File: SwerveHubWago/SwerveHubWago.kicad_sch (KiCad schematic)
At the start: 5 parts, among them J1 2601-1110, J2 2601-1104, J3 15-91-3024

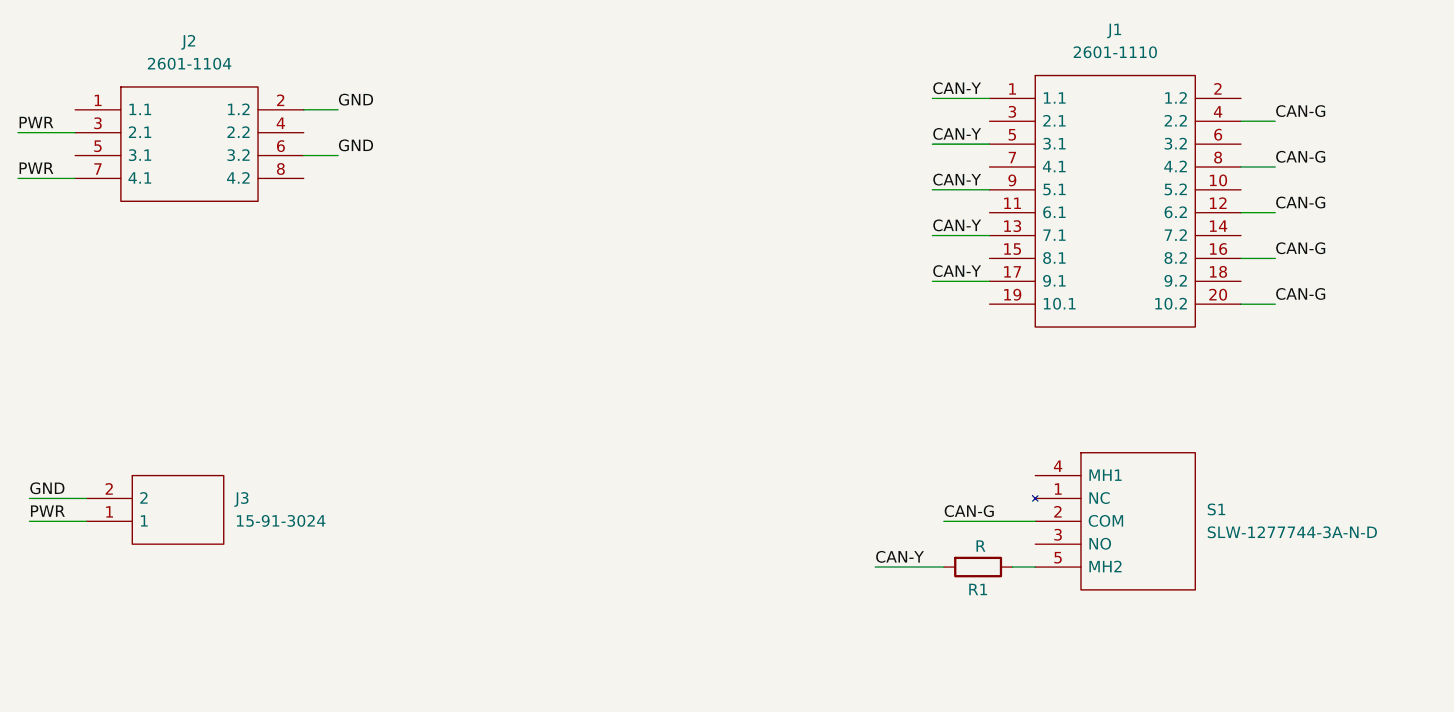
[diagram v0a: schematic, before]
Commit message: Rev 2
Switched connecters to two (in/out) Molex SL connectors for CAN and one three pin Molex SL connector for power. Changed Wago terminal blocks to 6 position for CAN and 2 position for power.
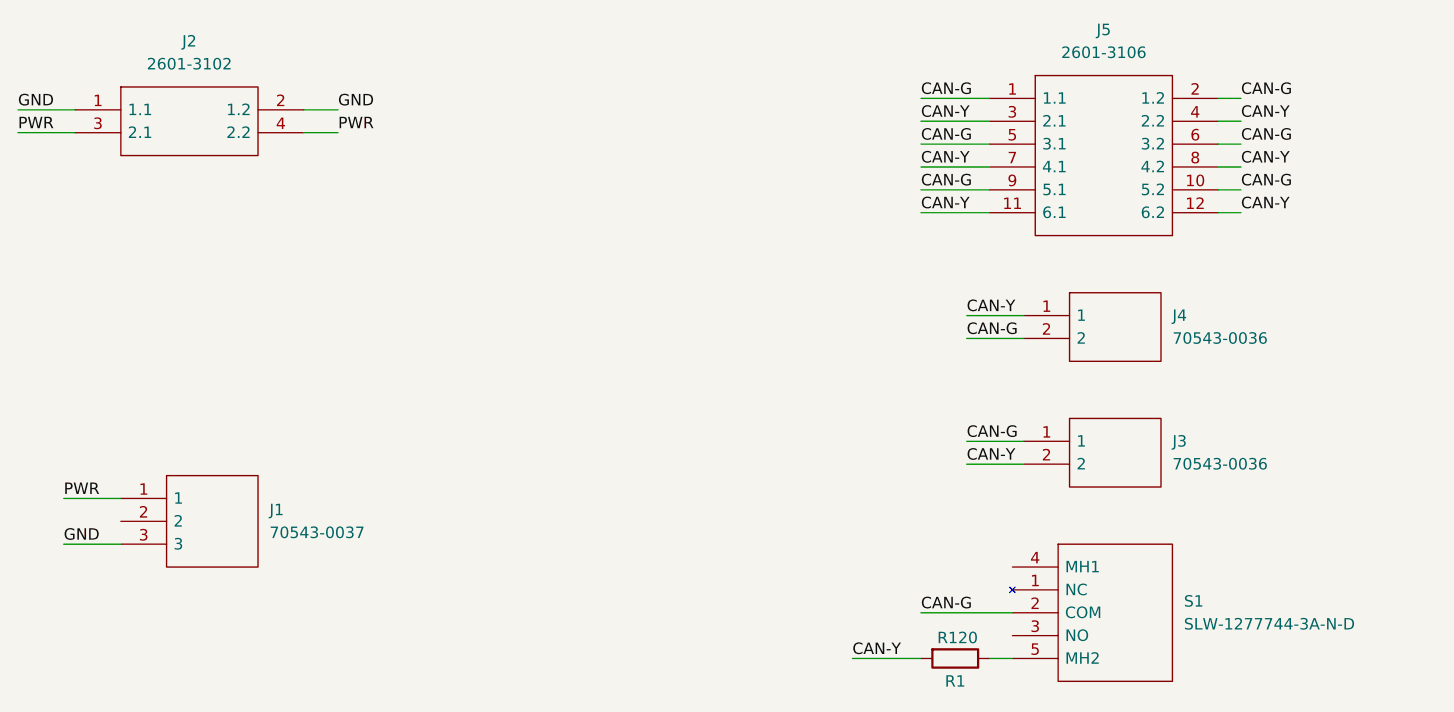
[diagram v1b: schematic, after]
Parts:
- removed J1: 2601-1110, SamacSys_Parts:26011110, symbol SamacSys_Parts:2601-1110
- removed J2: 2601-1104, SamacSys_Parts:26011104, symbol SamacSys_Parts:2601-1104
- removed J3: 15-91-3024, SamacSys_Parts:15913024, symbol SamacSys_Parts:15-91-3024
- added J1: 70543-0037, SamacSys_Parts:SHDR3W97P0X254_1X3_1017X660X1181P, symbol SamacSys_Parts:70543-0037
- added J2: 2601-3102, SamacSys_Parts:26013102, symbol SamacSys_Parts:2601-3102
- added J3, J4: 70543-0036, SamacSys_Parts:SHDR2W64P0X254_1X2_737X660X1194P, symbol SamacSys_Parts:70543-0036
- added J5: 2601-3106, SamacSys_Parts:26013106, symbol SamacSys_Parts:2601-3106
- R1: value R -> R120
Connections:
- net CAN-G: now also J3.1, J4.2, J5.1 (1.1), J5.10 (5.2), J5.2 (1.2), J5.5 (3.1), J5.6 (3.2), J5.9 (5.1)
- net CAN-Y: now also J3.2, J4.1, J5.11 (6.1), J5.12 (6.2), J5.3 (2.1), J5.4 (2.2), J5.7 (4.1), J5.8 (4.2)
- net GND: now also J1.3, J2.1 (1.1), J2.2 (1.2)
- net PWR: now also J1.1, J2.3 (2.1), J2.4 (2.2)
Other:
- moved on the sheet: R1, S1

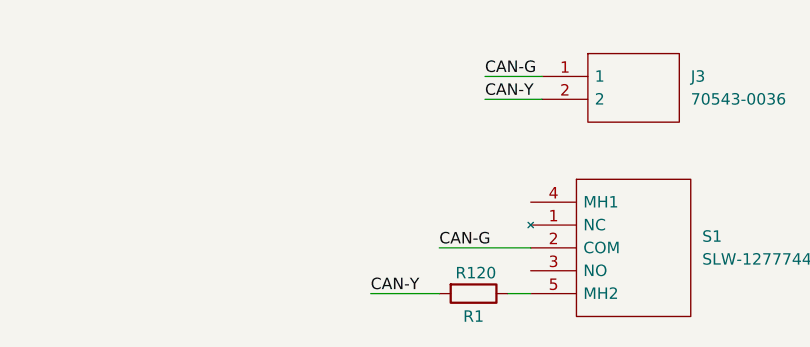
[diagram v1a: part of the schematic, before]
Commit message: Fixed switch connections
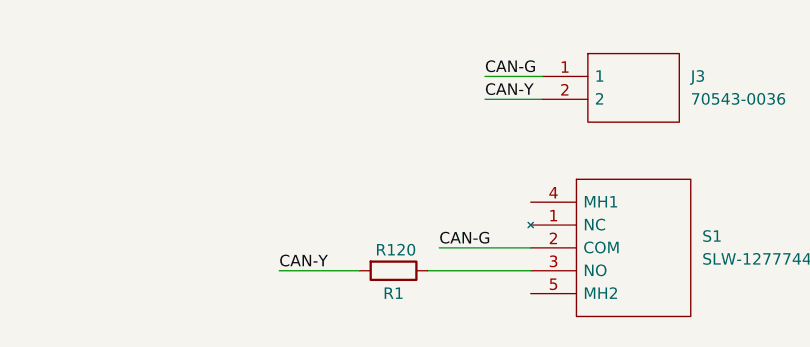
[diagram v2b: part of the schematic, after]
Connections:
- net at S1.3 (NO): now also R1.1
- net at S1.5 (MH2): no longer R1.1
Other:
- moved on the sheet: R1
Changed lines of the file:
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@@
 	(wire
 		(pts
-			(xy 161.29 128.27) (xy 168.91 128.27)
+			(xy 151.13 125.73) (xy 160.02 125.73)
 		)
 		(stroke
@@
 	(wire
 		(pts
-			(xy 176.53 128.27) (xy 179.07 128.27)
+			(xy 167.64 125.73) (xy 179.07 125.73)
 		)
 		(stroke
@@
 	)
 	(label "CAN-Y"
-		(at 161.29 128.27 0)
+		(at 151.13 125.73 0)
 		(fields_autoplaced yes)
 		(effects
@@
 	(symbol
 		(lib_id "Device:R")
-		(at 172.72 128.27 270)
+		(at 163.83 125.73 270)
 		(unit 1)
 		(exclude_from_sim no)
@@
 		(dnp no)
 		(property "Reference" "R1"
-			(at 172.72 130.81 90)
+			(at 163.83 128.27 90)
 			(effects
 				(font
@@
 		)
 		(property "Value" "R120"
-			(at 172.974 125.984 90)
+			(at 164.084 123.444 90)
 			(effects
 				(font
@@
 		)
 		(property "Footprint" "Resistor_SMD:R_0805_2012Metric_Pad1.20x1.40mm_HandSolder"
-			(at 172.72 126.492 90)
+			(at 163.83 123.952 90)
 			(effects
 				(font
@@
 		)
 		(property "Datasheet" "~"
-			(at 172.72 128.27 0)
+			(at 163.83 125.73 0)
 			(effects
 				(font
@@
 		)
 		(property "Description" "Resistor"
-			(at 172.72 128.27 0)
-			(effects
-				(font
+			(at 163.83 125.73 0)
+			(effects
+				(font
